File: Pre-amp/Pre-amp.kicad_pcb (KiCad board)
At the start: 2 copper layers, 182.9 x 53.3 mm, 131 parts, among them J1 In, J2 PWR, J3 Send, J4 Return, J5 Out, K1 G6H-2, Q1 J113 NJFET, Q2 J113 NJFET, Q3 J113 NJFET, Q4 J113 NJFET, SW1 Jack, SW2 Panel, U1 LF353N, U2 LF353N, U3 LF353N, U4 LF353N, U5 LF353N

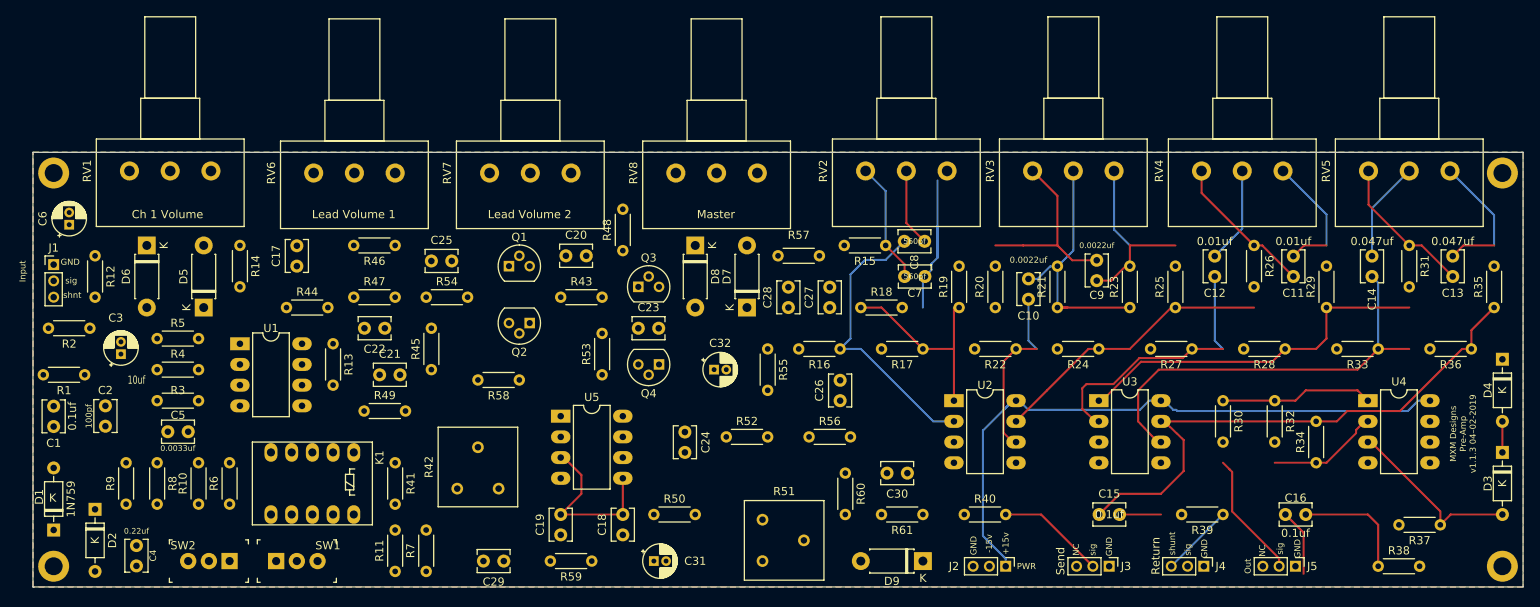
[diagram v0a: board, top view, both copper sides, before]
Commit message: connect all traces
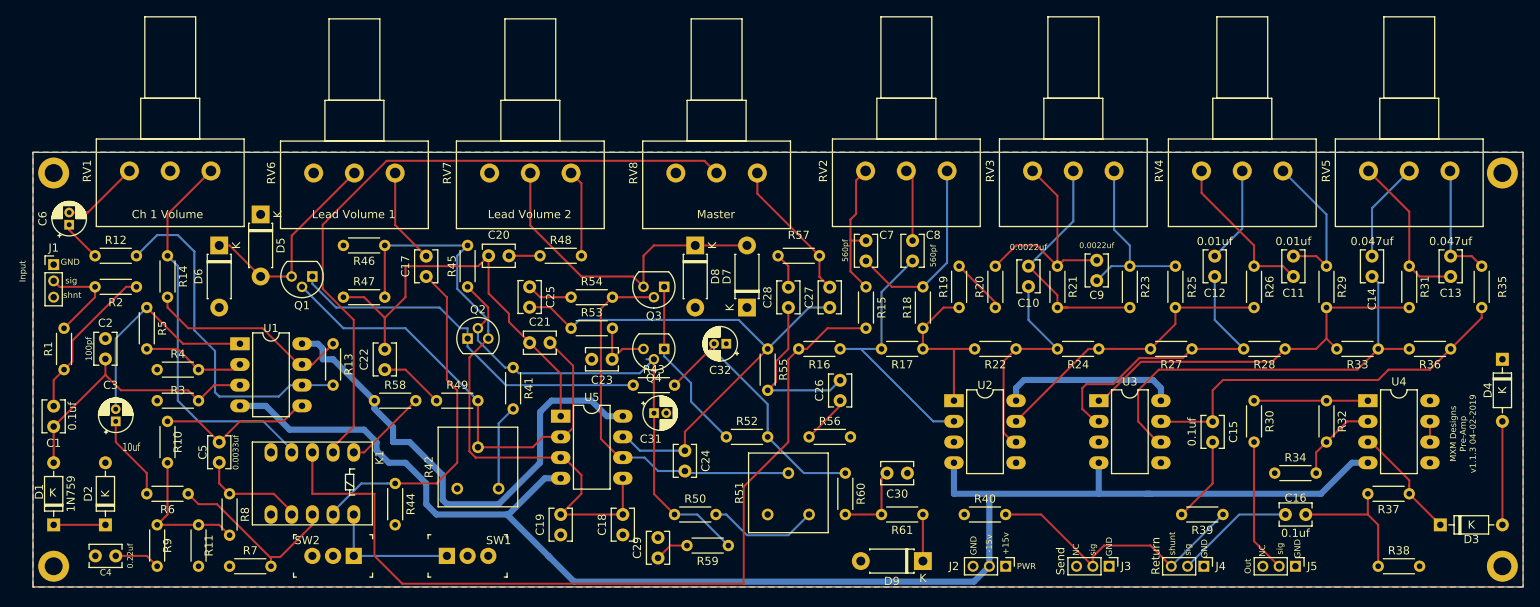
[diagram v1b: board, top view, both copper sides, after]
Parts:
- moved R44 25.4 mm to (95.2, 88.9), turned to 270 degrees
- moved Q1 24.2 mm to (85.1, 63.5), turned to 180 degrees
- moved R11 24.1 mm to (71.1, 99.1)
- moved R7 24.1 mm to (74.9, 99.1), turned to 0 degrees
- moved SW1 21.0 mm to (104.1, 97.8)
- moved C29 18.9 mm to (127.5, 98.0), turned to 90 degrees
- moved C21 18.8 mm to (111.8, 71.6)
- moved R41 18.6 mm to (109.7, 74.7)
- moved C31 18.2 mm to (127.0, 80.3)
- moved R58 18.0 mm to (92.7, 78.7), turned to 0 degrees
- moved R54 17.8 mm to (116.8, 66.0)
- moved R59 16.9 mm to (136.1, 96.5)
- moved C17 15.9 mm to (99.1, 63.5)
- moved SW2 15.3 mm to (87.6, 97.8)
- moved C15 14.5 mm to (195.6, 83.8), turned to 90 degrees
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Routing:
- net -15V: track 0.00 -> 182.9 mm
- net Net-(K1-Pad3): track 0.00 -> 108.0 mm
- net Net-(K1-Pad2): track 0.00 -> 82.8 mm
- net Net-(C24-Pad1): track 0.00 -> 66.9 mm
- net D: track 0.00 -> 61.3 mm
- net Net-(C21-Pad2): track 0.00 -> 57.4 mm
- net F: track 21.4 -> 77.8 mm
- net Net-(C20-Pad1): track 0.00 -> 51.5 mm
- net Net-(C24-Pad2): track 0.00 -> 47.8 mm
- net Net-(K1-Pad4): track 0.00 -> 47.7 mm
- net Net-(Q1-Pad1): track 0.00 -> 46.8 mm
- net Net-(R12-Pad2): track 0.00 -> 43.0 mm
- net Net-(C17-Pad1): track 0.00 -> 42.5 mm
- net Net-(D7-Pad2): track 0.00 -> 40.5 mm
- net Net-(C1-Pad1): track 0.00 -> 34.0 mm
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- added copper zone on F.Cu, net +15V
- added copper zone on B.Cu, net GND
- removed copper zone on B.Cu, net +15V
- removed copper zone on F.Cu, net GND

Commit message: clean up PCB
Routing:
- net Net-(C5-Pad1): track 13.3 -> 17.9 mm
- net Net-(C24-Pad1): track 66.9 -> 69.2 mm
- net Net-(K1-Pad3): track 108.0 -> 105.8 mm
- net Net-(D7-Pad2): track 40.5 -> 39.0 mm
- net Net-(C16-Pad1): track 14.6 -> 15.4 mm
- net E: track 32.6 -> 33.4 mm
- net Net-(K1-Pad2): track 82.8 -> 82.1 mm

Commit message: fx botch git commits
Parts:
- removed K1: G6H-2, Relay_THT:Relay_DPDT_Omron_G6H-2
- added C33: 1uF, Capacitors_THT:C_Disc_D3.8mm_W2.6mm_P2.50mm, F.Cu at (112.3, 98.0)
- added D10: LED, LEDs:LED_D3.0mm, F.Cu at (105.7, 97.5)
- added R62: 2.2k, Resistors_THT:R_Axial_DIN0204_L3.6mm_D1.6mm_P5.08mm_Horizontal, F.Cu at (101.6, 98.6)
- added R63: 470, Resistors_THT:R_Axial_DIN0204_L3.6mm_D1.6mm_P5.08mm_Horizontal, F.Cu at (114.3, 94.5)
- added R64: 1K, Resistors_THT:R_Axial_DIN0204_L3.6mm_D1.6mm_P5.08mm_Horizontal, F.Cu at (99.1, 97.5)
- added U6: DG419LDJ, Package_DIP:DIP-8_W7.62mm_LongPads, F.Cu at (78.7, 86.9)
- added U7: DG419LDJ, Package_DIP:DIP-8_W7.62mm_LongPads, F.Cu at (90.4, 86.9)
- H1, H2, H3, H4: footprint MountingHole:MountingHole_2.2mm_M2_DIN965_Pad -> Mounting_Holes:MountingHole_2.2mm_M2_DIN965_Pad
- R1, R10, R11, R12, R13, R14, R15, R16, R17, R18, R19, R2, R20, R21, R22, R23, R24, R25, R26, R27, R28, R29, R3, R30, R31, R32, R33, R34, R35, R36, R37, R38, R39, R4, R40, R41, R43, R44, R45, R46, R47, R48, R49, R5, R50, R52, R53, R54, R55, R56, R57, R58, R59, R6, R60, R61, R7, R8, R9: footprint Resistor_THT:R_Axial_DIN0204_L3.6mm_D1.6mm_P5.08mm_Horizontal -> Resistors_THT:R_Axial_DIN0204_L3.6mm_D1.6mm_P5.08mm_Horizontal
- RV1, RV2, RV3, RV4, RV5, RV6, RV7, RV8: footprint Potentiometer_THT:Potentiometer_Alps_RK163_Single_Horizontal -> Potentiometers:Potentiometer_Alps_RK163_Single_Vertical
- SW1, SW2: footprint digikey-footprints:Switch_Toggle_ATE1D-2M3-10-Z -> Pin_Headers:Pin_Header_Straight_1x03_Pitch2.00mm
- moved SW2 27.8 mm to (115.4, 98.6), turned to 90 degrees
- moved SW1 23.9 mm to (80.3, 98.6), turned to 270 degrees
- moved R58 19.1 mm to (89.4, 97.5), turned to 180 degrees
- moved R7 16.8 mm to (64.0, 86.4)
- moved R44 7.17 mm to (98.0, 82.3), turned to 180 degrees
- moved R10 4.23 mm to (65.0, 82.8), turned to 0 degrees
- moved C29 3.09 mm to (127.0, 95.0)
- moved C19 1.78 mm to (117.3, 92.7)
- moved R50 1.37 mm to (130.0, 91.4)
- moved R11 1.02 mm to (70.1, 99.1)
- moved R6 0.76 mm to (69.1, 90.2)
- moved R59 0.51 mm to (136.1, 96.0)
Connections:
- net Net-(C17-Pad1) renamed DIST-IN
- net Net-(C5-Pad1) renamed CLEAN-IN
- net Net-(K1-Pad3) renamed TONE-IN
- net Net-(K1-Pad4) renamed CLEAN-OUT
- J3 pad 3: Net-(J3-Pad3) -> (no net)
- J5 pad 3: Net-(J5-Pad3) -> (no net)
- R58 pad 1: +15V -> Net-(R58-Pad1)
- RV8 pad 2: Net-(K1-Pad2) -> DIST-OUT
- SW1 pad 3: Net-(SW1-Pad3) -> (no net)
- SW2 pad 3: Net-(SW2-Pad3) -> (no net)
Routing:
- net DIST-OUT: track 0.00 -> 85.1 mm
- net Net-(K1-Pad2): track 82.1 -> 0.00 mm
- net +15V: track 83.5 -> 21.7 mm
- net Net-(C33-Pad1): track 16.5 -> 55.4 mm
- net Net-(R58-Pad1): track 0.00 -> 17.5 mm
- net DIST-IN: track 42.5 -> 26.5 mm
- net Net-(R6-Pad1): track 22.5 -> 29.1 mm
- net Net-(R58-Pad2): track 10.3 -> 3.89 mm
- net CLEAN-IN: track 17.9 -> 23.2 mm
- net -15V: track 182.9 -> 188.2 mm
- net Net-(R10-Pad1): track 17.6 -> 21.6 mm
- net Net-(D10-Pad2): track 0.00 -> 3.77 mm
- net Net-(C5-Pad2): track 19.4 -> 16.0 mm
- net TONE-IN: track 105.8 -> 108.8 mm
- net Net-(C24-Pad1): track 69.2 -> 66.9 mm
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
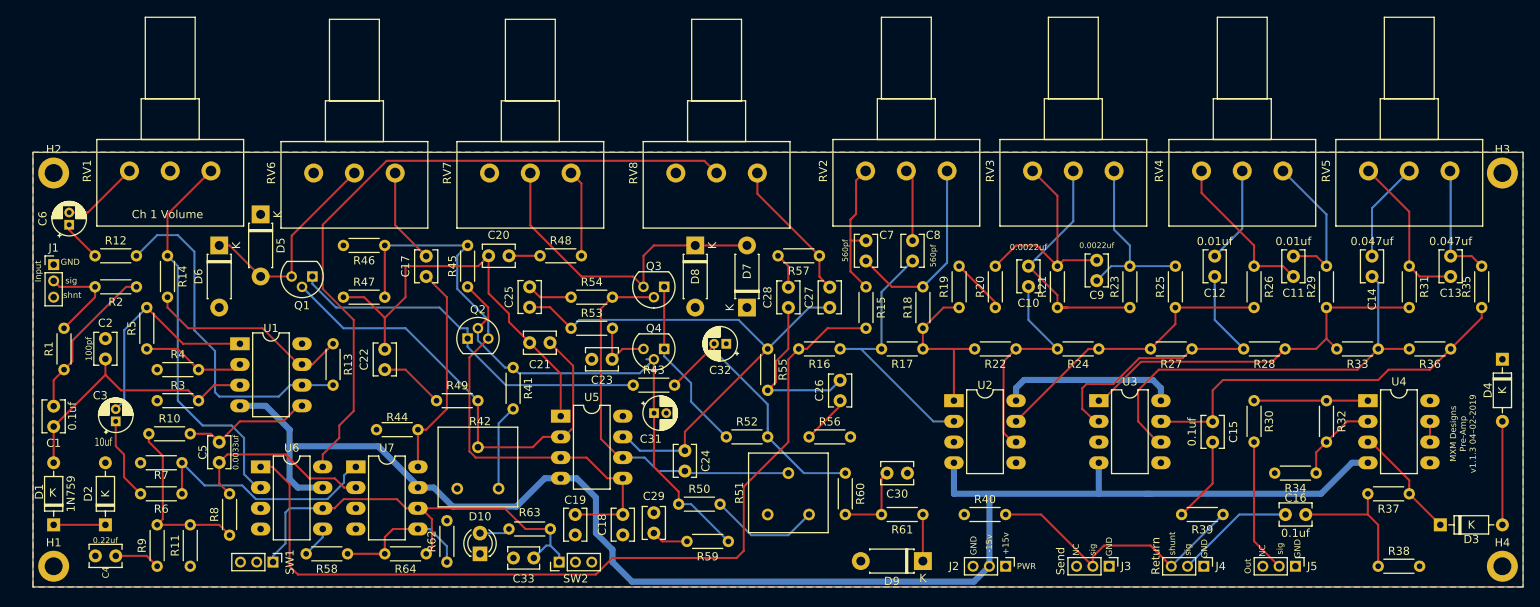
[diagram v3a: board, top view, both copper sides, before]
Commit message: spread out components better.
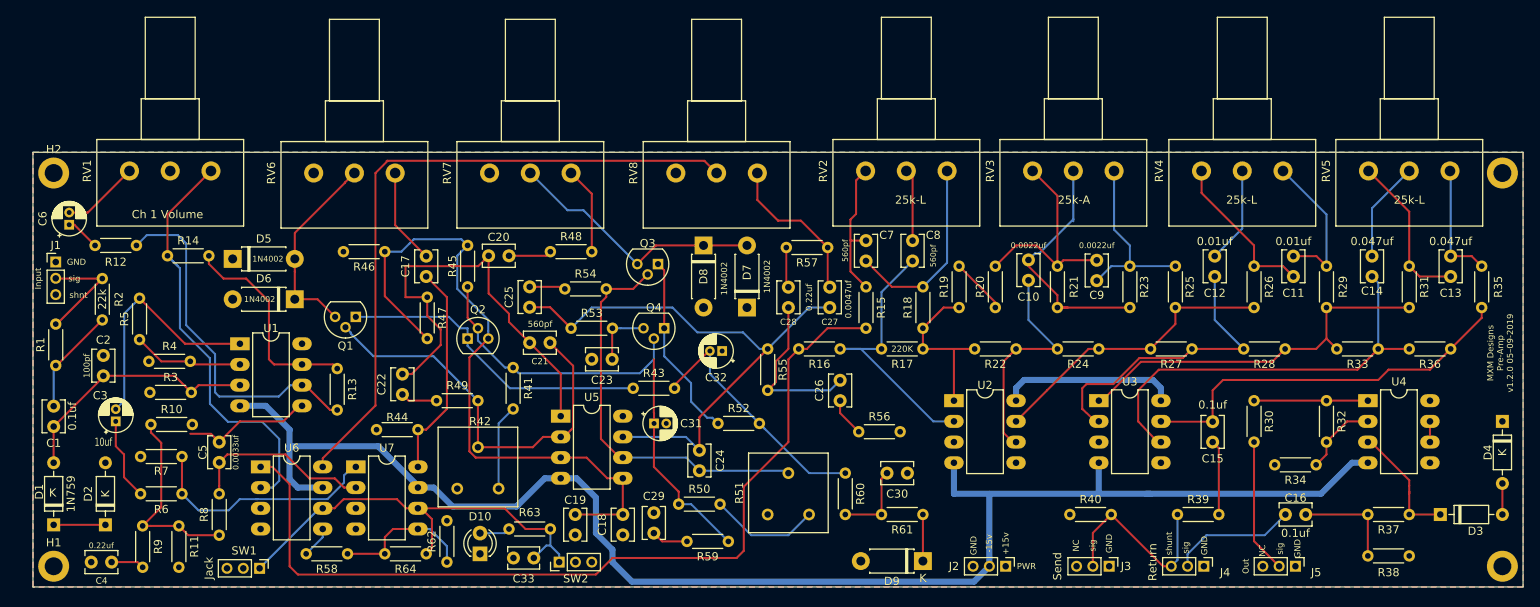
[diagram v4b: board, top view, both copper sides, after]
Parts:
- moved R40 13.0 mm to (178.1, 92.7)
- moved D6 11.4 mm to (82.9, 66.3), turned to 180 degrees
- moved R47 10.3 mm to (99.2, 66.0), turned to 270 degrees
- moved D4 7.62 mm to (231.1, 81.3)
- moved Q1 7.28 mm to (90.4, 68.5)
- moved D5 6.45 mm to (75.3, 61.3), turned to 0 degrees
- moved R56 6.13 mm to (152.1, 82.5)
- moved R2 5.84 mm to (59.3, 68.8), turned to 90 degrees
- moved R39 5.59 mm to (191.3, 92.7), turned to 0 degrees
- moved C22 3.74 mm to (96.1, 78.0)
- moved R13 3.09 mm to (88.1, 74.8)
- moved Q3 2.90 mm to (127.5, 62.0)
- moved Q4 2.54 mm to (128.3, 69.8)
- moved R37 2.54 mm to (219.7, 92.7)
- moved C2 2.09 mm to (59.4, 73.2)
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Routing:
- net Net-(J3-Pad2): track 34.7 -> 23.9 mm
- net Net-(D3-Pad2): track 12.7 -> 3.81 mm
- net Net-(Q1-Pad1): track 46.8 -> 38.9 mm
- net F: track 75.7 -> 83.1 mm
- net Net-(C21-Pad2): track 57.4 -> 50.1 mm
- net Net-(D7-Pad2): track 40.5 -> 33.2 mm
- net Net-(C1-Pad2): track 19.6 -> 13.1 mm
- net CLEAN-OUT: track 48.1 -> 52.8 mm
- net Net-(C16-Pad2): track 17.0 -> 12.7 mm
- net Net-(C22-Pad1): track 7.93 -> 4.51 mm
- net DIST-OUT: track 85.1 -> 82.0 mm
- net Net-(C24-Pad1): track 66.9 -> 69.6 mm
- net Net-(C1-Pad1): track 34.0 -> 31.4 mm
- net Net-(R10-Pad1): track 21.6 -> 23.8 mm
- net Net-(C3-Pad2): track 27.3 -> 29.5 mm
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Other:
- board text added: "MXM Designs Pre-Amp v1.2.0 05–09-2019"
- board text removed: "MXM Designs Pre-Amp v1.1.3 04–02-2019"
